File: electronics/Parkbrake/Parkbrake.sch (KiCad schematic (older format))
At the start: 28 parts, among them P1 Conn48pin, Q1 BSS138, Q2 BSS138, Q3 P-ch -40V 0.0035ohm, Q4 P-ch -40V 0.0035ohm, Q5 BSS308, Q6 BSS308

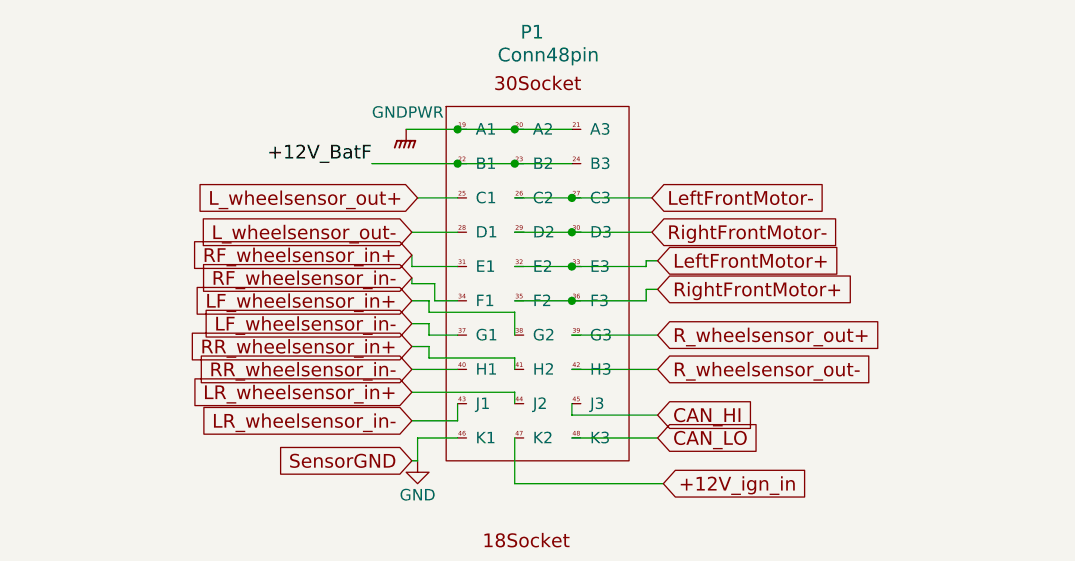
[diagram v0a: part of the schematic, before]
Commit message: Front motors H-bridge finished
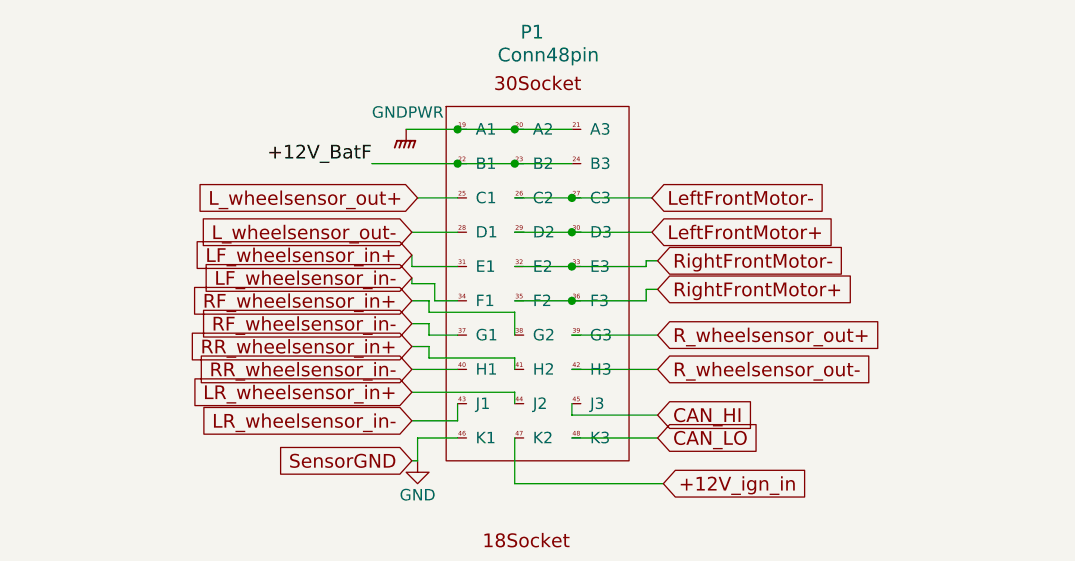
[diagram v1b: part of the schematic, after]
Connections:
- net LF_wheelsensor_in+: now also P1.31 (E1); no longer P1.38 (G2)
- net LF_wheelsensor_in-: now also P1.34 (F1); no longer P1.37 (G1)
- net LeftFrontMotor+: now also P1.29 (D2), P1.30 (D3); no longer P1.32 (E2), P1.33 (E3)
- net RF_wheelsensor_in+: now also P1.38 (G2); no longer P1.31 (E1)
- net RF_wheelsensor_in-: now also P1.37 (G1); no longer P1.34 (F1)
- net RightFrontMotor-: now also P1.32 (E2), P1.33 (E3); no longer P1.29 (D2), P1.30 (D3)
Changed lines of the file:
@@
 $EndComp
 $Comp
-L GND #PWR8
+L GND #PWR01
 U 1 1 5708DE8A
 P 4750 7250
-F 0 "#PWR8" H 4750 7000 50  0001 C CNN
+F 0 "#PWR01" H 4750 7000 50  0001 C CNN
 F 1 "GND" H 4758 7077 50  0000 C CNN
 F 2 "" H 4750 7250 50  0000 C CNN
@@
 $EndComp
 $Comp
-L GNDPWR #PWR1
+L GNDPWR #PWR02
 U 1 1 57090A02
 P 1050 5775
-F 0 "#PWR1" H 1050 5575 50  0001 C CNN
+F 0 "#PWR02" H 1050 5575 50  0001 C CNN
 F 1 "GNDPWR" H 1057 5849 50  0001 C CNN
 F 2 "" H 1050 5725 50  0000 C CNN
@@
 $EndComp
 $Comp
-L GNDPWR #PWR3
+L GNDPWR #PWR03
 U 1 1 5701F17D
 P 1675 5075
-F 0 "#PWR3" H 1675 4875 50  0001 C CNN
+F 0 "#PWR03" H 1675 4875 50  0001 C CNN
 F 1 "GNDPWR" H 1682 5149 50  0001 C CNN
 F 2 "" H 1675 5025 50  0000 C CNN
@@
 $EndComp
 $Comp
-L GND #PWR9
+L GND #PWR04
 U 1 1 570200C5
 P 5375 7050
-F 0 "#PWR9" H 5375 6800 50  0001 C CNN
+F 0 "#PWR04" H 5375 6800 50  0001 C CNN
 F 1 "GND" H 5383 6877 50  0000 C CNN
 F 2 "" H 5375 7050 50  0000 C CNN
@@
 $EndComp
 $Comp
-L GNDPWR #PWR5
+L GNDPWR #PWR05
 U 1 1 570235BF
 P 2025 1075
-F 0 "#PWR5" H 2025 875 50  0001 C CNN
+F 0 "#PWR05" H 2025 875 50  0001 C CNN
 F 1 "GNDPWR" H 2032 1149 50  0000 C CNN
 F 2 "" H 2025 1025 50  0000 C CNN
@@
 Text Label 1875 1225 2    60   ~ 0
 +12V_BatF
-Text GLabel 3125 1650 2    60   Input ~ 0
+Text GLabel 3100 1525 2    60   Input ~ 0
 LeftFrontMotor+
 Text GLabel 3100 1375 2    60   Input ~ 0
@@
 Text GLabel 3125 1775 2    60   Input ~ 0
 RightFrontMotor+
-Text GLabel 3100 1525 2    60   Input ~ 0
+Text GLabel 3125 1650 2    60   Input ~ 0
 RightFrontMotor-
 Text GLabel 3100 3375 2    60   Input ~ 0
@@
 $EndSheet
 $Comp
-L GND #PWR7
+L GND #PWR06
 U 1 1 578E7EF2
 P 2075 2525
-F 0 "#PWR7" H 2075 2275 50  0001 C CNN
+F 0 "#PWR06" H 2075 2275 50  0001 C CNN
 F 1 "GND" H 2075 2375 50  0000 C CNN
 F 2 "" H 2075 2525 50  0000 C CNN
@@
 	1    0    0    -1
 $EndComp
-Text GLabel 2050 1825 0    60   Input ~ 0
+Text GLabel 2050 1625 0    60   Input ~ 0
 LF_wheelsensor_in+
-Text GLabel 2050 1925 0    60   Input ~ 0
+Text GLabel 2050 1725 0    60   Input ~ 0
 LF_wheelsensor_in-
 Text GLabel 2050 2350 0    60   Input ~ 0
@@
 Text GLabel 2050 2225 0    60   Input ~ 0
 LR_wheelsensor_in+
-Text GLabel 2050 1725 0    60   Input ~ 0
+Text GLabel 2050 1925 0    60   Input ~ 0
 RF_wheelsensor_in-
-Text GLabel 2050 1625 0    60   Input ~ 0
+Text GLabel 2050 1825 0    60   Input ~ 0
 RF_wheelsensor_in+
 Text GLabel 2050 2125 0    60   Input ~ 0
@@
 L_wheelsensor_out+
 $Comp
-L PWR_FLAG #FLG1
+L PWR_FLAG #FLG07
 U 1 1 578EA974
 P 1150 4575
-F 0 "#FLG1" H 1150 4670 50  0001 C CNN
+F 0 "#FLG07" H 1150 4670 50  0001 C CNN
 F 1 "PWR_FLAG" H 1150 4755 50  0000 C CNN
 F 2 "" H 1150 4575 50  0000 C CNN
@@
 $EndComp
 $Comp
-L PWR_FLAG #FLG7
+L PWR_FLAG #FLG08
 U 1 1 578EAB0E
 P 4425 6550
-F 0 "#FLG7" H 4425 6645 50  0001 C CNN
+F 0 "#FLG08" H 4425 6645 50  0001 C CNN
 F 1 "PWR_FLAG" H 4425 6730 50  0001 C CNN
 F 2 "" H 4425 6550 50  0000 C CNN
@@
 $EndComp
 $Comp
-L PWR_FLAG #FLG9
+L PWR_FLAG #FLG09
 U 1 1 578EAB3C
 P 5375 7050
-F 0 "#FLG9" H 5375 7145 50  0001 C CNN
+F 0 "#FLG09" H 5375 7145 50  0001 C CNN
 F 1 "PWR_FLAG" H 5375 7250 50  0001 C CNN
 F 2 "" H 5375 7050 50  0000 C CNN
@@
 ParkbrakeSwitch_non_invert
 $Comp
-L PWR_FLAG #FLG6
+L PWR_FLAG #FLG010
 U 1 1 578F074A
 P 4425 6125
-F 0 "#FLG6" H 4425 6220 50  0001 C CNN
+F 0 "#FLG010" H 4425 6220 50  0001 C CNN
 F 1 "PWR_FLAG" H 4425 6305 50  0001 C CNN
 F 2 "" H 4425 6125 50  0000 C CNN
@@
 $EndComp
 $Comp
-L PWR_FLAG #FLG8
+L PWR_FLAG #FLG011
 U 1 1 5797B077
 P 5375 6550
-F 0 "#FLG8" H 5375 6645 50  0001 C CNN
+F 0 "#FLG011" H 5375 6645 50  0001 C CNN
 F 1 "PWR_FLAG" H 5375 6750 50  0001 C CNN
 F 2 "" H 5375 6550 50  0000 C CNN
@@
 $EndComp
 $Comp
-L PWR_FLAG #FLG3
+L PWR_FLAG #FLG012
 U 1 1 579735F3
 P 1675 4575
-F 0 "#FLG3" H 1675 4670 50  0001 C CNN
+F 0 "#FLG012" H 1675 4670 50  0001 C CNN
 F 1 "PWR_FLAG" H 1700 4775 50  0001 C CNN
 F 2 "" H 1675 4575 50  0000 C CNN
@@
 $EndComp
 $Comp
-L GNDPWR #PWR6
+L GNDPWR #PWR013
 U 1 1 579818E3
 P 2025 3825
-F 0 "#PWR6" H 2025 3625 50  0001 C CNN
+F 0 "#PWR013" H 2025 3625 50  0001 C CNN
 F 1 "GNDPWR" H 2025 3700 50  0000 C CNN
 F 2 "" H 2025 3775 50  0000 C CNN
@@
 $EndComp
 $Comp
-L GNDPWR #PWR2
+L GNDPWR #PWR014
 U 1 1 5798E6D1
 P 1050 7575
-F 0 "#PWR2" H 1050 7375 50  0001 C CNN
+F 0 "#PWR014" H 1050 7375 50  0001 C CNN
 F 1 "GNDPWR" H 1057 7649 50  0001 C CNN
 F 2 "" H 1050 7525 50  0000 C CNN
@@
 $EndComp
 $Comp
-L GNDPWR #PWR4
+L GNDPWR #PWR015
 U 1 1 5798E6F2
 P 1675 6875
-F 0 "#PWR4" H 1675 6675 50  0001 C CNN
+F 0 "#PWR015" H 1675 6675 50  0001 C CNN
 F 1 "GNDPWR" H 1682 6949 50  0001 C CNN
 F 2 "" H 1675 6825 50  0000 C CNN
@@
 Batt switch off and polarity protection
 $Comp
-L PWR_FLAG #FLG2
+L PWR_FLAG #FLG016
 U 1 1 5798E6F9
 P 1150 6375
-F 0 "#FLG2" H 1150 6470 50  0001 C CNN
+F 0 "#FLG016" H 1150 6470 50  0001 C CNN
 F 1 "PWR_FLAG" H 1150 6555 50  0000 C CNN
 F 2 "" H 1150 6375 50  0000 C CNN
@@
 $EndComp
 $Comp
-L PWR_FLAG #FLG5
+L PWR_FLAG #FLG017
 U 1 1 5798E6FF
 P 1675 6875
-F 0 "#FLG5" H 1675 6970 50  0001 C CNN
+F 0 "#FLG017" H 1675 6970 50  0001 C CNN
 F 1 "PWR_FLAG" H 1700 7075 50  0001 C CNN
 F 2 "" H 1675 6875 50  0000 C CNN
@@
 $EndComp
 $Comp
-L PWR_FLAG #FLG4
+L PWR_FLAG #FLG018
 U 1 1 5798E705
 P 1675 6375
-F 0 "#FLG4" H 1675 6470 50  0001 C CNN
+F 0 "#FLG018" H 1675 6470 50  0001 C CNN
 F 1 "PWR_FLAG" H 1700 6575 50  0001 C CNN
 F 2 "" H 1675 6375 50  0000 C CNN

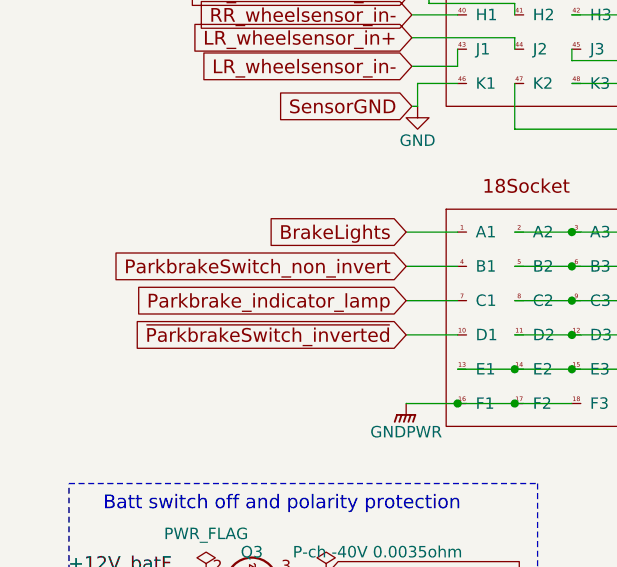
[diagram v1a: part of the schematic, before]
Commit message: More work on inputs and 5 volt
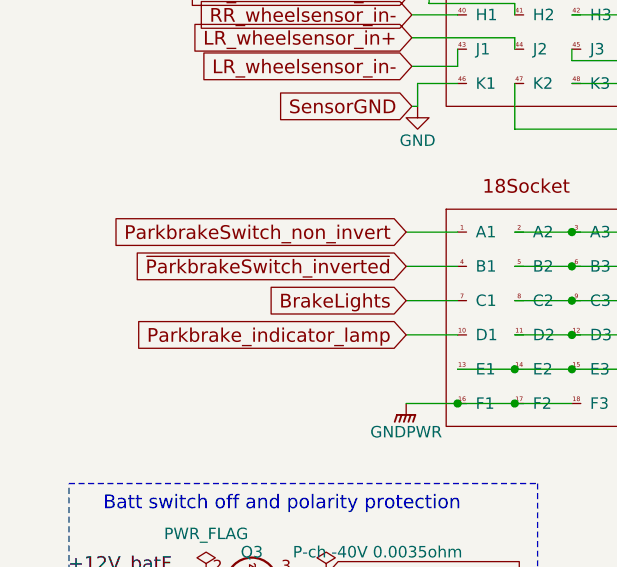
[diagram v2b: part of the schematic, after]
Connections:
- net BrakeLights: now also P1.7 (C1); no longer P1.1 (A1)
- net ParkbrakeSwitch_non_invert: now also P1.1 (A1); no longer P1.4 (B1)
- net Parkbrake_indicator_lamp: now also P1.10 (D1); no longer P1.7 (C1)
- net ~ParkbrakeSwitch_inverted: now also P1.4 (B1); no longer P1.10 (D1)
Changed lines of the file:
@@
 Text GLabel 2050 2025 0    60   Input ~ 0
 RR_wheelsensor_in+
+Text GLabel 2025 3525 0    60   Input ~ 0
+Parkbrake_indicator_lamp
 Text GLabel 2025 3375 0    60   Input ~ 0
-Parkbrake_indicator_lamp
+BrakeLights
 Text GLabel 2025 3075 0    60   Input ~ 0
-BrakeLights
+ParkbrakeSwitch_non_invert
 Text GLabel 2025 3225 0    60   Input ~ 0
-ParkbrakeSwitch_non_invert
-Text GLabel 2025 3525 0    60   Input ~ 0
 ~ParkbrakeSwitch_inverted
 Text GLabel 3125 2125 2    60   Input ~ 0

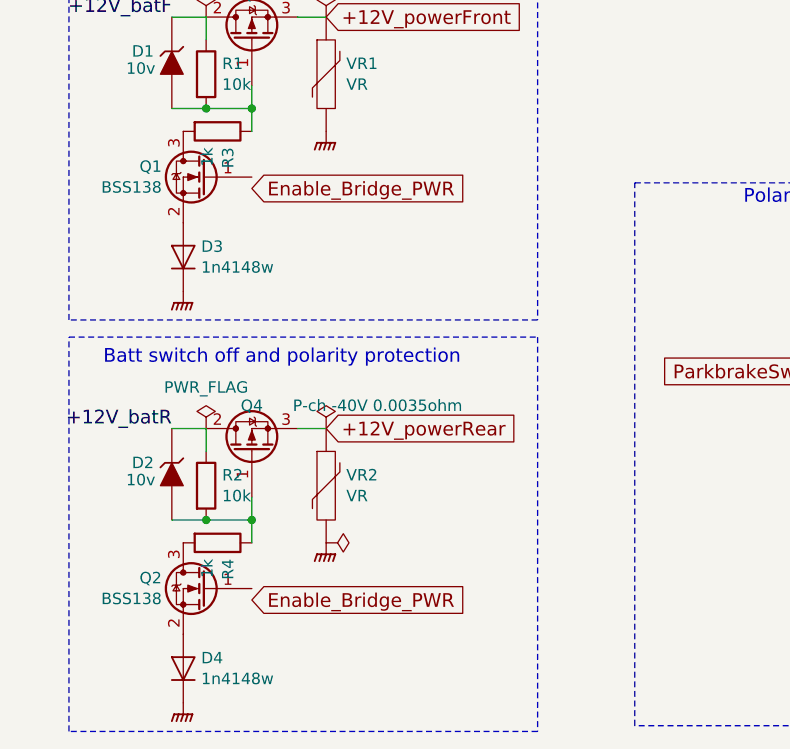
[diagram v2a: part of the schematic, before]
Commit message: minor tweaks to pcb, had a cap on wrong polarity
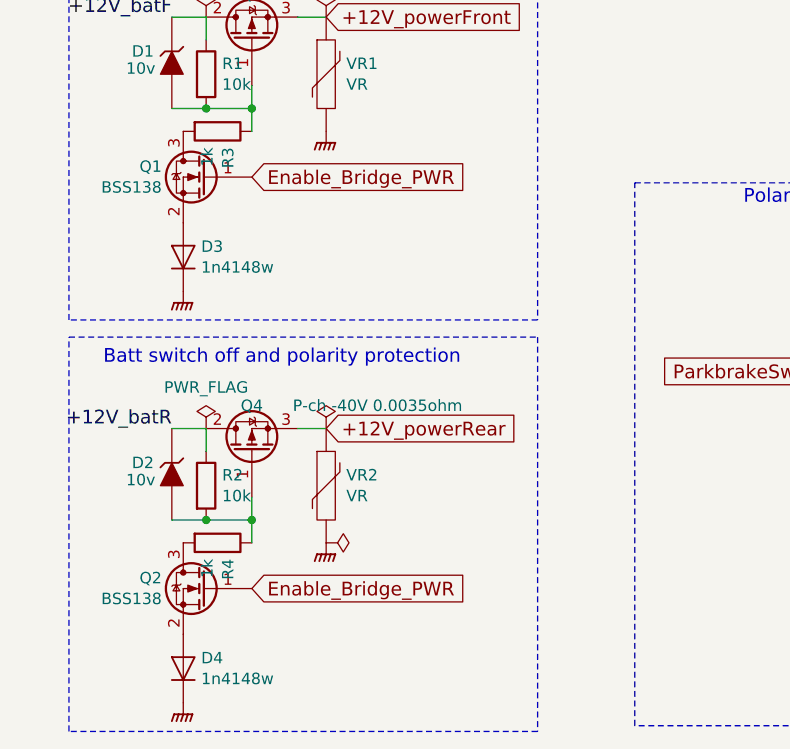
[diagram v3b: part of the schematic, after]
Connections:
- net Enable_Bridge_PWR: now also Q1.1 (G), Q2.1 (G)
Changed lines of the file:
@@
 Text GLabel 1675 4575 2    60   Input ~ 0
 +12V_powerFront
-Text GLabel 1350 5325 2    60   Input ~ 0
+Text GLabel 1350 5275 2    60   Input ~ 0
 Enable_Bridge_PWR
 Text GLabel 5425 6550 2    60   Input ~ 0
@@
 Text GLabel 1675 6375 2    60   Input ~ 0
 +12V_powerRear
-Text GLabel 1350 7125 2    60   Input ~ 0
+Text GLabel 1350 7075 2    60   Input ~ 0
 Enable_Bridge_PWR
 $Comp
